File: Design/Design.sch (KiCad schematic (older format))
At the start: 8 parts, among them U1 LM393

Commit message: Slightly modified the design
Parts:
- added C?: 0.33uF, symbol C_Small
- added C?: 0.1uF, symbol C_Small
- added D3: SR1100, symbol SR1100
- added L1: INDUCTOR, symbol INDUCTOR
- added Q1: PSMN022-30PL, TO-220AB, symbol PSMN022-30PL
- added R6, R?: 1k, symbol R
- added R7: 1.5, symbol R
- added R?: IAT, symbol RVAR
- added R?: MAP, symbol RVAR
- added U?: LM7805, symbol LM7805
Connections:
- net labels added: +12V, IAT, TRIG
- wire segments 18 -> 33
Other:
- note added: "Coil / injector driver"
- note added: "Intake temperature sensor\nvoltage divider"

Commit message: Deleted some old reference photo, modified the arduino code to fire some sparks [works with IRF840], updated the design - now the VRS conditioning circuit is working
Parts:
- R3: value 4.7k -> 2k
- R4: value 5.1k -> 3k
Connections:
- net labels added: VSR_GR, VSR_WY
- net labels removed: VSR_CAM_PIN_1, VSR_CAM_PIN_2
- wire segments 33 -> 36
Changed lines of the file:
@@
 LIBS:microchip_dspic33dsc
 LIBS:pspice
-LIBS:phoenix
-LIBS:cvra
-LIBS:_wireless
-LIBS:_transceiver
-LIBS:_stm32
-LIBS:_sensors
-LIBS:_power
-LIBS:_motor_drivers
-LIBS:_linear-regulators
-LIBS:_ic
-LIBS:_div
-LIBS:_connectors
-LIBS:_charge-pump-regulators
-LIBS:_audio
-LIBS:_antenna
-LIBS:National
-LIBS:Mec
-LIBS:IRF
-LIBS:Comp2014
 LIBS:logo
 LIBS:Design-cache
@@
 $EndComp
 Text GLabel 1750 900  0    60   Input ~ 0
-VSR_CAM_PIN_1
+VSR_GR
 Text GLabel 1850 1650 0    60   Input ~ 0
-VSR_CAM_PIN_2
+VSR_WY
 $Comp
 L SR1100 D2
@@
 Connection ~ 2250 1650
 Wire Wire Line
-	1750 900  3000 900
+	1750 900  2900 900
 Wire Wire Line
 	2250 600  2250 1350
@@
 Wire Wire Line
 	1850 1650 2250 1650
-Wire Wire Line
-	3000 900  3000 1450
 $Comp
 L R R4
@@
 P 2600 1800
 F 0 "R4" V 2680 1800 50  0000 C CNN
-F 1 "5.1k" V 2600 1800 50  0000 C CNN
+F 1 "3k" V 2600 1800 50  0000 C CNN
 F 2 "" V 2530 1800 50  0000 C CNN
 F 3 "" H 2600 1800 50  0000 C CNN
@@
 P 2600 1400
 F 0 "R3" V 2680 1400 50  0000 C CNN
-F 1 "4.7k" V 2600 1400 50  0000 C CNN
+F 1 "2k" V 2600 1400 50  0000 C CNN
 F 2 "" V 2530 1400 50  0000 C CNN
 F 3 "" H 2600 1400 50  0000 C CNN
@@
 	2600 1550 2600 1650
 Connection ~ 2600 1650
-Wire Wire Line
-	2600 1650 3000 1650
 Wire Wire Line
 	3200 2000 3200 1850
@@
 	2600 1950 2600 2000
 Wire Wire Line
-	2250 2150 2250 1950
+	2250 1950 2250 2150
 $Comp
 L GND-RESCUE-Design #PWR2
@@
 $EndComp
 $Comp
-L GND #PWR4
+L GND-RESCUE-Design #PWR4
 U 1 1 570C1BBD
 P 2500 4250
@@
 	5300 2750 5300 2900
 $Comp
-L GND #PWR?
+L GND-RESCUE-Design #PWR?
 U 1 1 570DCAC8
 P 5300 3400
@@
 	1    0    0    -1
 $EndComp
+Wire Wire Line
+	3000 1450 2800 1450
+Wire Wire Line
+	2800 1450 2800 1650
+Wire Wire Line
+	2800 1650 2600 1650
+Wire Wire Line
+	3000 1650 2900 1650
+Wire Wire Line
+	2900 1650 2900 900
 $EndSCHEMATC

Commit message: Updated the design schematic according to the breadboarded rectifier done on Apr 13 2016. Added the picture of schematic
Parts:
- removed D1, D2: SR1100, symbol SR1100
- removed Q1: PSMN022-30PL, TO-220AB, symbol PSMN022-30PL
- removed R1, R2, R5: 1k, symbol R
- removed R3: 2k, symbol R
- removed R4: 3k, symbol R
- removed U1: LM393, symbol LM393
- added D? (x4): SR1100, symbol SR1100
- added Q?: IRF840, TO-220AB, symbol IRF840
- added R?: 10k, symbol R
- added R? (x3): 1k, symbol R
- added U? (x2): LM393, symbol LM393
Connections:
- net labels added: +BATT, IAT_OUT, VRS0_HIGH, VRS0_LOW, VRS0_OUT, VRS1_HIGH, VRS1_LOW, VRS1_OUT, VRS_TH
- net labels removed: +12V, CAM_BIN, IAT, VSR_GR, VSR_WY
- wire segments 36 -> 29
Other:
- note added: "VRS conditioning as a half-cycle rectifiers\nused for zero crossing detection"
- moved on the sheet: C?, R?, U?

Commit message: Timed spark at different cylinders
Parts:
- added 0.01pF: C, symbol C
- added 10k: R, symbol R
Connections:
- net labels added: VRS_OUT
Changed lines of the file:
@@
 LIBS:microchip_dspic33dsc
 LIBS:pspice
-LIBS:phoenix
-LIBS:cvra
-LIBS:_wireless
-LIBS:_transceiver
-LIBS:_stm32
-LIBS:_sensors
-LIBS:_power
-LIBS:_motor_drivers
-LIBS:_linear-regulators
-LIBS:_ic
-LIBS:_div
-LIBS:_connectors
-LIBS:_charge-pump-regulators
-LIBS:_audio
-LIBS:_antenna
-LIBS:National
-LIBS:Mec
-LIBS:IRF
-LIBS:Comp2014
 LIBS:logo
 LIBS:Design-cache
@@
 	1100 1100 900  1100
 $Comp
-L GND #PWR?
+L GND-RESCUE-Design #PWR?
 U 1 1 570FFE0E
 P 900 1400
@@
 Connection ~ 3000 1250
 $Comp
-L GND #PWR?
+L GND-RESCUE-Design #PWR?
 U 1 1 57101C04
 P 3000 1550
@@
 	1500 1800 1200 1800
 $Comp
-L GND #PWR?
+L GND-RESCUE-Design #PWR?
 U 1 1 5710466B
 P 1500 1850
@@
 	2800 1250 3750 1250
 $Comp
-L GND #PWR?
+L GND-RESCUE-Design #PWR?
 U 1 1 57109002
 P 3950 1650
@@
 Connection ~ 3000 2200
 $Comp
-L GND #PWR?
+L GND-RESCUE-Design #PWR?
 U 1 1 5710CE0E
 P 3000 2500
@@
 	2800 2200 3750 2200
 $Comp
-L GND #PWR?
+L GND-RESCUE-Design #PWR?
 U 1 1 5710CE1C
 P 3950 2600
@@
 Text Notes 4500 750  2    60   ~ 0
 VRS conditioning as a half-cycle rectifiers\nused for zero crossing detection
+$Comp
+L C 0.01pF
+U 1 1 57118ACC
+P 6750 2350
+F 0 "0.01pF" H 6775 2450 50  0000 L CNN
+F 1 "C" H 6775 2250 50  0000 L CNN
+F 2 "" H 6788 2200 50  0000 C CNN
+F 3 "" H 6750 2350 50  0000 C CNN
+	1    6750 2350
+	1    0    0    -1
+$EndComp
+$Comp
+L R 10k
+U 1 1 57118BBF
+P 6600 2200
+F 0 "10k" V 6680 2200 50  0000 C CNN
+F 1 "R" V 6600 2200 50  0000 C CNN
+F 2 "" V 6530 2200 50  0000 C CNN
+F 3 "" H 6600 2200 50  0000 C CNN
+	1    6600 2200
+	0    1    1    0
+$EndComp
+$Comp
+L GND #PWR?
+U 1 1 57118D68
+P 6750 2500
+F 0 "#PWR?" H 6750 2250 50  0001 C CNN
+F 1 "GND" H 6750 2350 50  0000 C CNN
+F 2 "" H 6750 2500 50  0000 C CNN
+F 3 "" H 6750 2500 50  0000 C CNN
+	1    6750 2500
+	1    0    0    -1
+$EndComp
+Text GLabel 6450 2200 0    60   Input ~ 0
+VRS_OUT
+Connection ~ 6750 2200
 $EndSCHEMATC

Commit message: Added the megasquirt schematics to the ref
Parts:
- added U?: MKE06Z128VLD4, symbol MKE06Z128VLD4
- C1: renamed from C?; value 0.33uF -> 10uF
- C2: renamed from C?; value 0.1uF -> 10uF
- R3, R4: renamed from R?; value 1k -> 10k
- R6: value 1k -> 10k
- gave numbers to parts that had none: 12
- renumbered 0.01pF to 0.01pF1
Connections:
- wire segments 29 -> 40
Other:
- moved on the sheet: R5, R8, R9

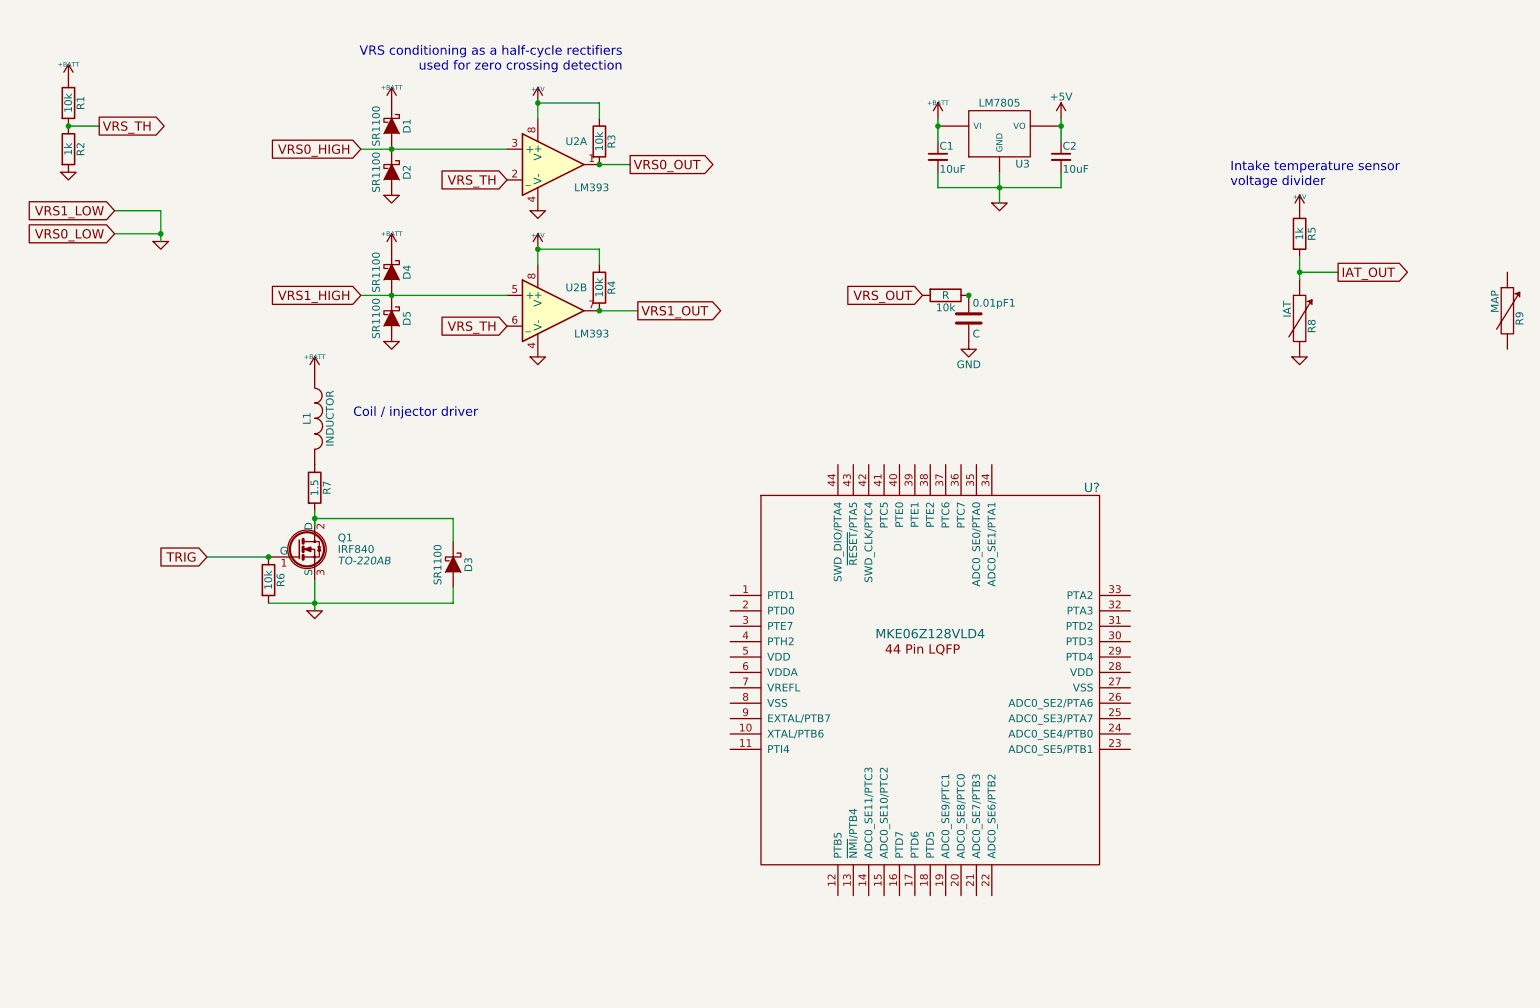
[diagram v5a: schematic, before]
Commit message: Slight modifications to the schematics, added protection zeners
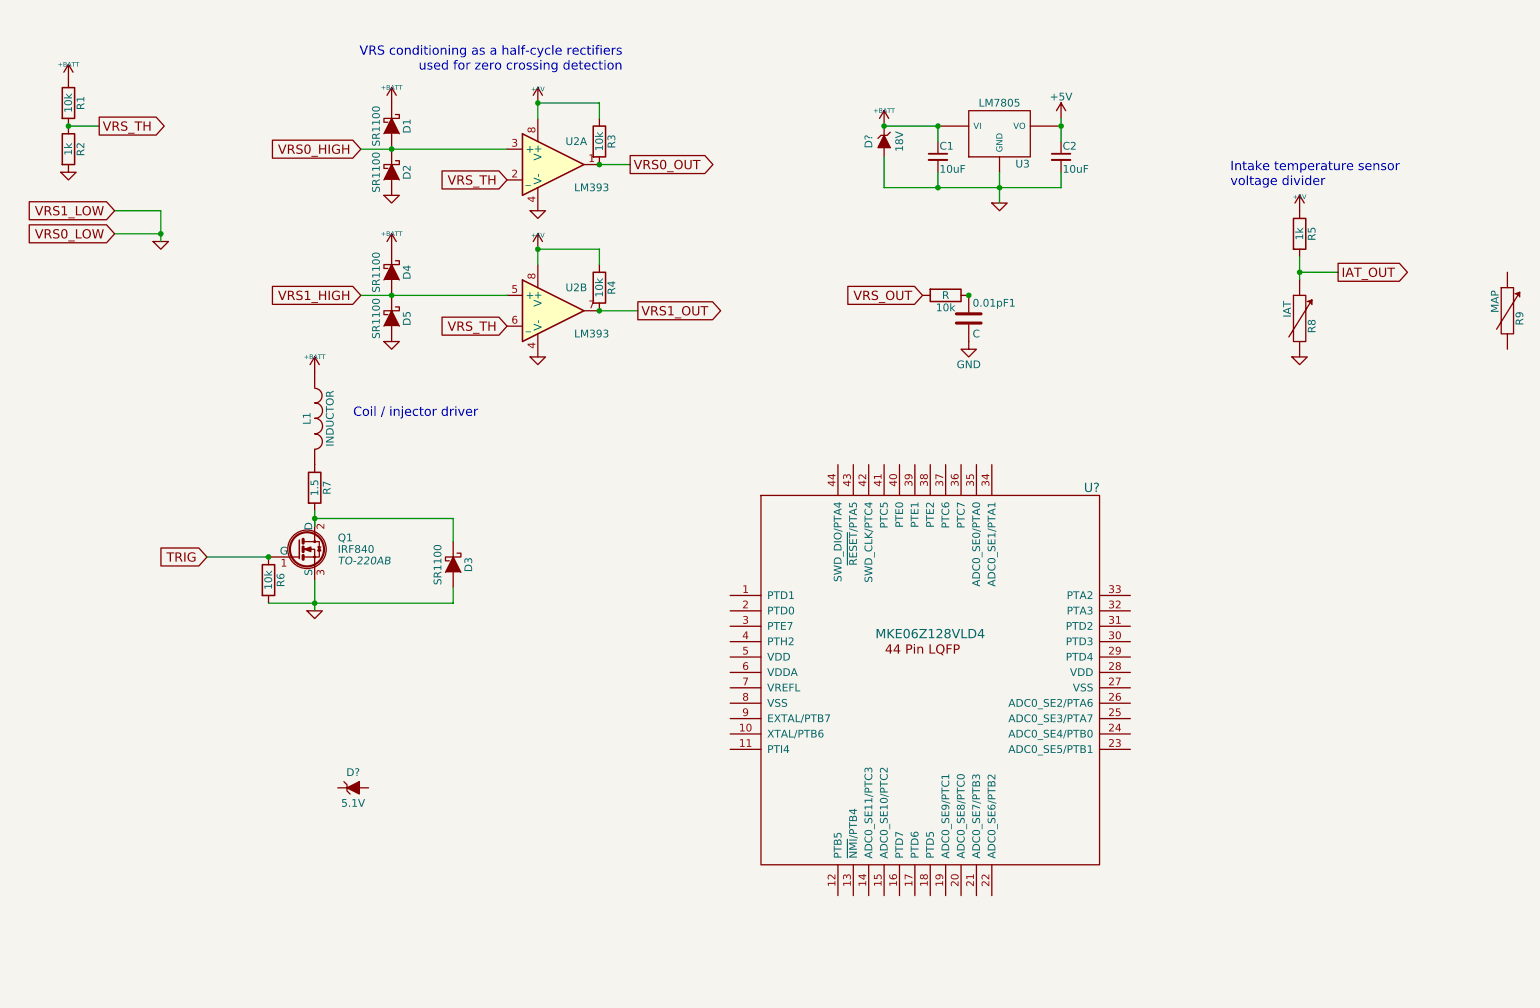
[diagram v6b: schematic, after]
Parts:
- added 18V: D?, symbol ZENERsmall
- added D?: 5.1V, symbol ZENERsmall
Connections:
- net +BATT: now also 18V.1 (K)
- net GND: now also 18V.2 (A)
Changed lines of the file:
@@
 $EndComp
 Wire Wire Line
-	2500 4050 2500 4200
-Wire Wire Line
-	2500 4200 2500 4250
+	2500 4050 2500 4250
 $Comp
 L R R6
@@
 $EndComp
 Wire Wire Line
-	2200 4200 2500 4200
-Wire Wire Line
-	2500 4200 3400 4200
+	2200 4200 3400 4200
 Connection ~ 2500 4200
 $Comp
@@
 	3400 3650 3400 3800
 Wire Wire Line
-	2500 3600 2500 3650
-Wire Wire Line
-	2500 3650 2500 3700
+	2500 3600 2500 3700
 Connection ~ 2500 3650
 Text Notes 2750 3000 0    60   ~ 0
@@
 $EndComp
 Wire Wire Line
-	6550 1050 6550 1100
-Wire Wire Line
-	6550 1100 6550 1200
-Connection ~ 6550 1100
-Wire Wire Line
 	6550 1400 6550 1500
 Wire Wire Line
-	6550 1500 6950 1500
-Wire Wire Line
-	6950 1500 7350 1500
-Wire Wire Line
-	6950 1400 6950 1500
-Wire Wire Line
-	6950 1500 6950 1600
+	6200 1500 7350 1500
+Wire Wire Line
+	6950 1400 6950 1600
 Connection ~ 6950 1500
 $Comp
@@
 $EndComp
 Wire Wire Line
-	7350 1050 7350 1100
-Wire Wire Line
-	7350 1100 7350 1200
+	7350 1050 7350 1200
 Wire Wire Line
 	7350 1500 7350 1400
@@
 $EndComp
 Wire Wire Line
-	8900 1950 8900 2050
-Wire Wire Line
-	8900 2050 8900 2100
+	8900 1950 8900 2100
 $Comp
 L GND-RESCUE-Design #PWR05
@@
 	1200 1650 1500 1650
 Wire Wire Line
-	1500 1650 1500 1800
-Wire Wire Line
-	1500 1800 1500 1850
+	1500 1650 1500 1850
 Wire Wire Line
 	1500 1800 1200 1800
@@
 VRS0_HIGH
 Wire Wire Line
-	2800 1250 3000 1250
-Wire Wire Line
-	3000 1250 3750 1250
+	2800 1250 3750 1250
 $Comp
 L GND-RESCUE-Design #PWR010
@@
 VRS1_HIGH
 Wire Wire Line
-	2800 2200 3000 2200
-Wire Wire Line
-	3000 2200 3750 2200
+	2800 2200 3750 2200
 $Comp
 L GND-RESCUE-Design #PWR014
@@
 L +BATT #PWR017
 U 1 1 571183A3
-P 6550 1050
-F 0 "#PWR017" H 6550 1000 20  0001 C CNN
-F 1 "+BATT" H 6550 1150 30  0000 C CNN
-F 2 "" H 6550 1050 60  0000 C CNN
-F 3 "" H 6550 1050 60  0000 C CNN
-	1    6550 1050
+P 6200 1100
+F 0 "#PWR017" H 6200 1050 20  0001 C CNN
+F 1 "+BATT" H 6200 1200 30  0000 C CNN
+F 2 "" H 6200 1100 60  0000 C CNN
+F 3 "" H 6200 1100 60  0000 C CNN
+	1    6200 1100
 	1    0    0    -1
 $EndComp
@@
 	1    0    0    -1
 $EndComp
+$Comp
+L ZENERsmall D?
+U 1 1 5718A5FC
+P 2750 5400
+F 0 "D?" H 2750 5500 50  0000 C CNN
+F 1 "5.1V" H 2750 5300 50  0000 C CNN
+F 2 "" H 2750 5400 50  0000 C CNN
+F 3 "" H 2750 5400 50  0000 C CNN
+	1    2750 5400
+	1    0    0    -1
+$EndComp
+$Comp
+L ZENERsmall 18V
+U 1 1 571883F8
+P 6200 1200
+F 0 "18V" H 6200 1300 50  0000 C CNN
+F 1 "D?" H 6200 1100 50  0000 C CNN
+F 2 "" H 6200 1200 50  0000 C CNN
+F 3 "" H 6200 1200 50  0000 C CNN
+	1    6200 1200
+	0    1    1    0
+$EndComp
+Wire Wire Line
+	6200 1500 6200 1300
+Connection ~ 6550 1500
+Wire Wire Line
+	6200 1100 6550 1100
+Wire Wire Line
+	6550 1100 6550 1200
+Connection ~ 6550 1100
+Connection ~ 6200 1100
 $EndSCHEMATC
